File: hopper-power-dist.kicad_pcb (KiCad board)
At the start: 2 copper layers, 28 parts, among them J1 XT90PW-M, J2 B2B-XH-A(LF)(SN), J3 XT60PW-F, J4 XT60PW-F, J5 XT60PW-F, J6 XT60PW-F, J7 XT60PW-F, J8 B2B-XH-A(LF)(SN), SW2 FT_Power_Switch

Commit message: Create basic PCB layout
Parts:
- added D5: LED, LED_SMD:LED_0603_1608Metric, F.Cu at (99.5, 116.0)
- added R4: 22kΩ, Resistor_SMD:R_0603_1608Metric_Pad0.98x0.95mm_HandSolder, F.Cu at (95.3, 116.0)
- added REF**: MountingHole_2.2mm_M2, MountingHole:MountingHole_2.2mm_M2, F.Cu at (59.0, 67.0)
- added REF**: MountingHole_2.2mm_M2, MountingHole:MountingHole_2.2mm_M2, F.Cu at (160.0, 138.0)
- added REF**: MountingHole_2.2mm_M2, MountingHole:MountingHole_2.2mm_M2, F.Cu at (160.0, 67.0)
- added REF**: MountingHole_2.2mm_M2, MountingHole:MountingHole_2.2mm_M2, F.Cu at (59.0, 138.0)
- moved J2 99.2 mm to (76.0, 68.0), turned to -90 degrees
- moved R2 83.3 mm to (90.6, 138.0)
- moved C9 80.1 mm to (97.5, 69.5), turned to 90 degrees
- moved D2 76.3 mm to (101.0, 126.8), turned to -90 degrees
- moved J1 76.2 mm to (145.0, 125.0)
- moved J5 72.9 mm to (72.8, 120.2), turned to -90 degrees
- moved R3 71.4 mm to (95.6, 130.4), turned to -90 degrees
- moved R1 68.8 mm to (101.0, 130.8), turned to -90 degrees
- moved J8 64.7 mm to (117.5, 129.0), turned to 180 degrees
- moved SW2 55.0 mm to (128.8, 123.2), turned to -90 degrees
- moved C5 54.9 mm to (97.5, 80.2), turned to 180 degrees
- moved S1 54.3 mm to (110.0, 117.0), turned to -90 degrees
- moved C7 48.7 mm to (115.9, 69.5), turned to 90 degrees
- moved D4 37.3 mm to (95.6, 126.2), turned to -90 degrees
- moved J6 37.0 mm to (147.8, 102.7), turned to 90 degrees
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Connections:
- J3 pad S1: Net-(J3-PadS1) -> GND
- J3 pad S2: Net-(J3-PadS1) -> GND
- J4 pad S1: Net-(J4-PadS1) -> GND
- J4 pad S2: Net-(J4-PadS1) -> GND
- J5 pad S1: Net-(J5-PadS1) -> GND
- J5 pad S2: Net-(J5-PadS1) -> GND
- J6 pad S1: Net-(J6-PadS1) -> GND
- J6 pad S2: Net-(J6-PadS1) -> GND
- J7 pad S1: Net-(J7-PadS1) -> GND
- J7 pad S2: Net-(J7-PadS1) -> GND
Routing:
- net Net-(J1-PadP): track 0.00 -> 12.9 mm
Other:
- board outline added: 109 x 79 mm

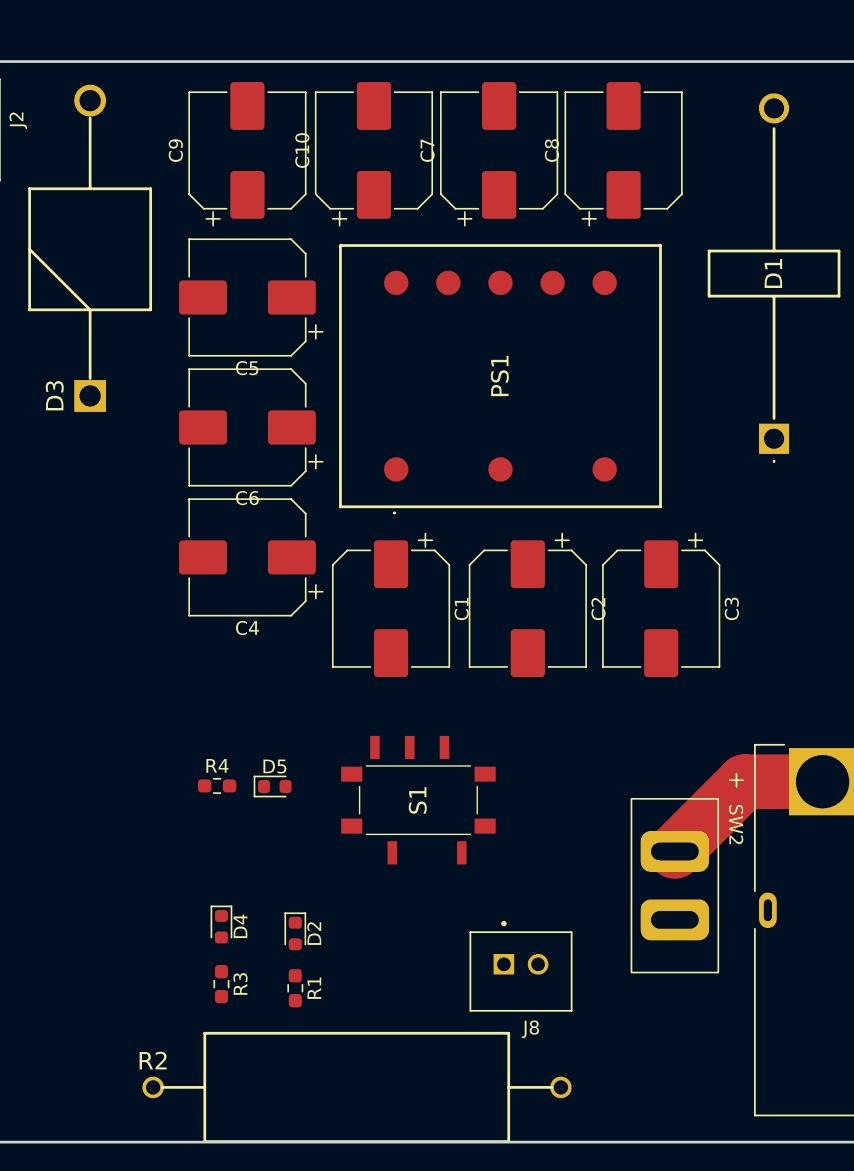
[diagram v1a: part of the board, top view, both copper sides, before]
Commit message: Fix schematic and update 3d models
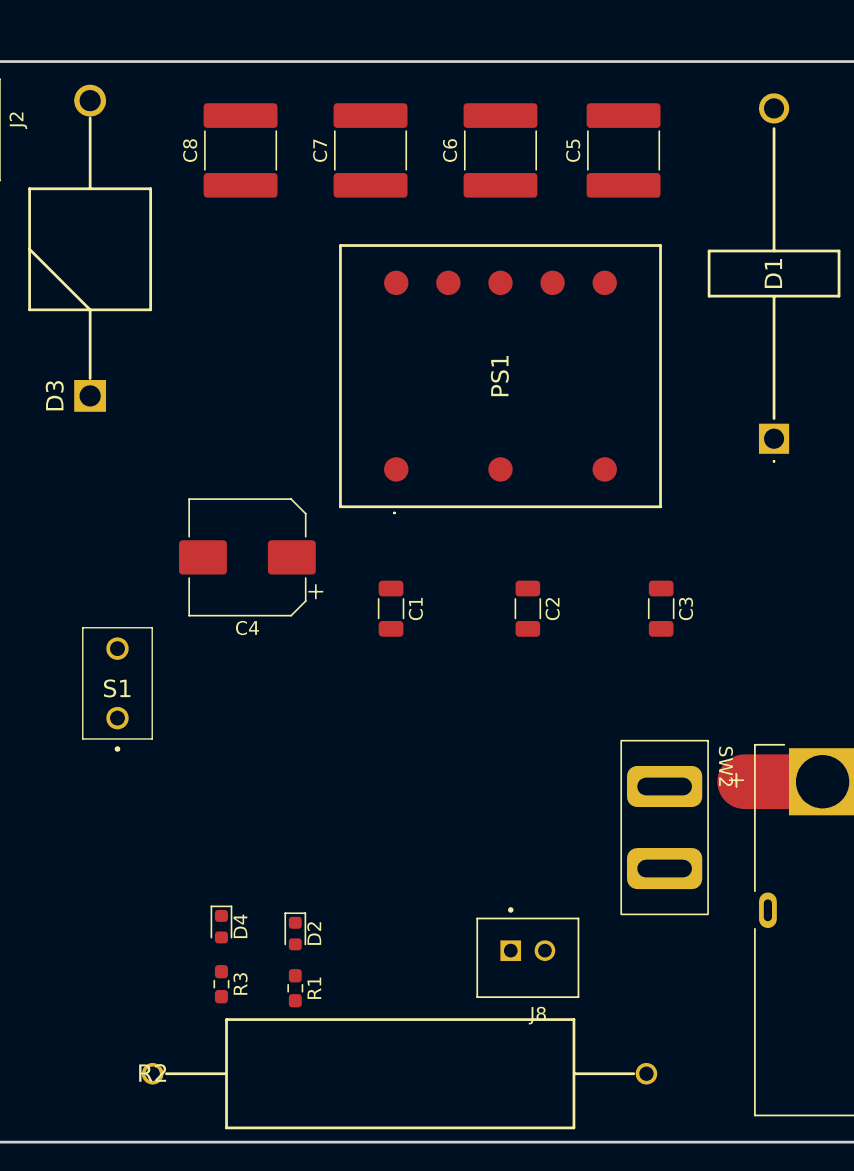
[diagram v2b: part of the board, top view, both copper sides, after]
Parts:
- removed the C5 at (97.5, 80.2)
- removed the C6 at (97.5, 89.8)
- removed D5: LED, LED_SMD:LED_0603_1608Metric
- removed R4: 22kΩ, Resistor_SMD:R_0603_1608Metric_Pad0.98x0.95mm_HandSolder
- C1, C2, C3: footprint Capacitor_SMD:CP_Elec_8x10 -> Capacitor_SMD:C_1206_3216Metric
- C5: renamed from C7; footprint Capacitor_SMD:CP_Elec_8x10 -> Capacitor_SMD:C_2220_5650Metric
- C6: renamed from C8; footprint Capacitor_SMD:CP_Elec_8x10 -> Capacitor_SMD:C_2220_5650Metric
- C7: renamed from C9; footprint Capacitor_SMD:CP_Elec_8x10 -> Capacitor_SMD:C_2220_5650Metric
- C8: renamed from C10; footprint Capacitor_SMD:CP_Elec_8x10 -> Capacitor_SMD:C_2220_5650Metric
- R2: footprint SamacSys_Parts:RESAD5390W86L2222D792 -> benbokser:CW005900R0JB12
- S1: value G3T12AB -> 2MS6T1B3M2QES; footprint SamacSys_Parts:G3T12AB -> SamacSys_Parts:2MS6T1B3M2QES
- moved S1 22.8 mm to (88.0, 111.0), turned to 0 degrees
- moved C8 9.75 mm to (97.0, 69.5)
- moved C5 9.10 mm to (125.0, 69.5)
- moved C6 9.00 mm to (116.0, 69.5)
- moved C7 9.00 mm to (106.5, 69.5)
- moved SW2 4.32 mm to (128.0, 119.0)
- moved J8 1.12 mm to (118.0, 128.0)
- moved R2 1.00 mm to (90.6, 137.0)
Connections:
- S1 pad 1: /HS -> GND
- S1 pad 3: GND -> Net-(PS1-Pad2)
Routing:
- net Net-(J1-PadP): track 12.9 -> 5.70 mm

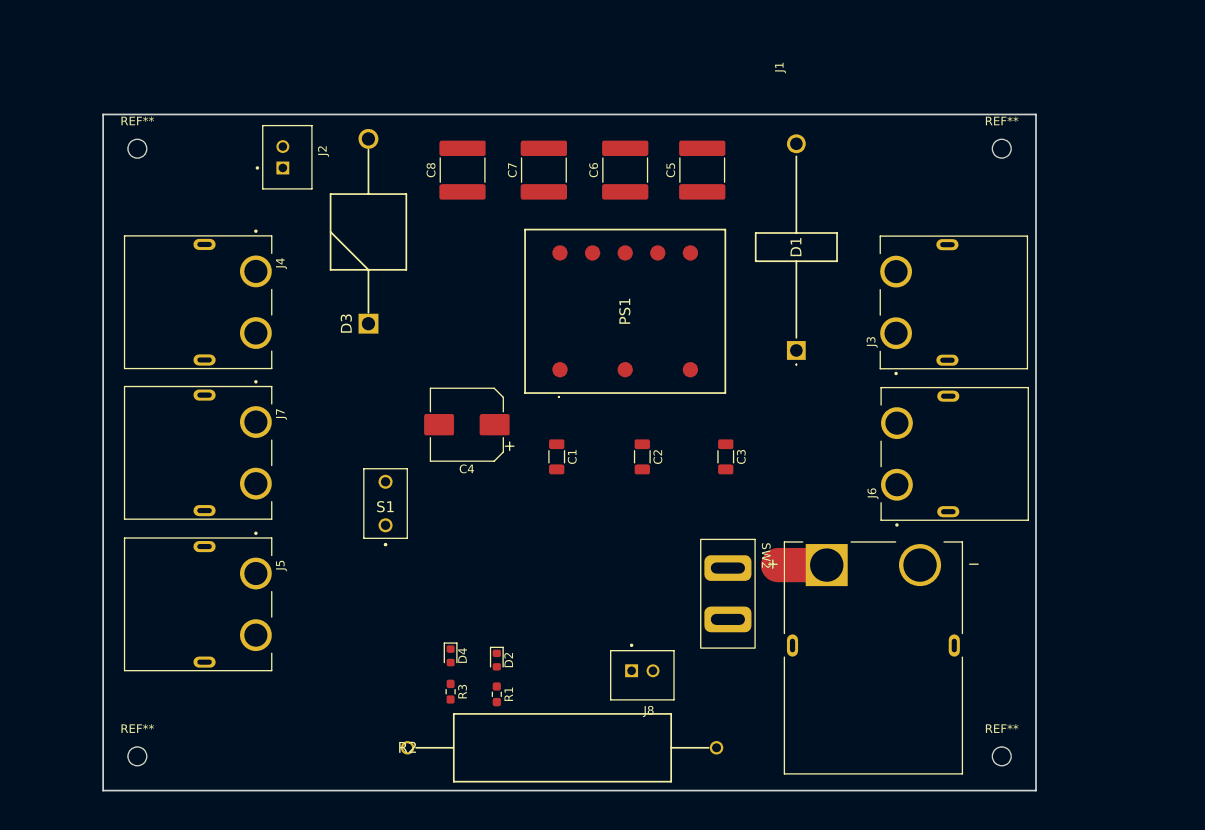
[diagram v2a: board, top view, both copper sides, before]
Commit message: Changed precharge resistor, routed PCB traces and updated 3D models
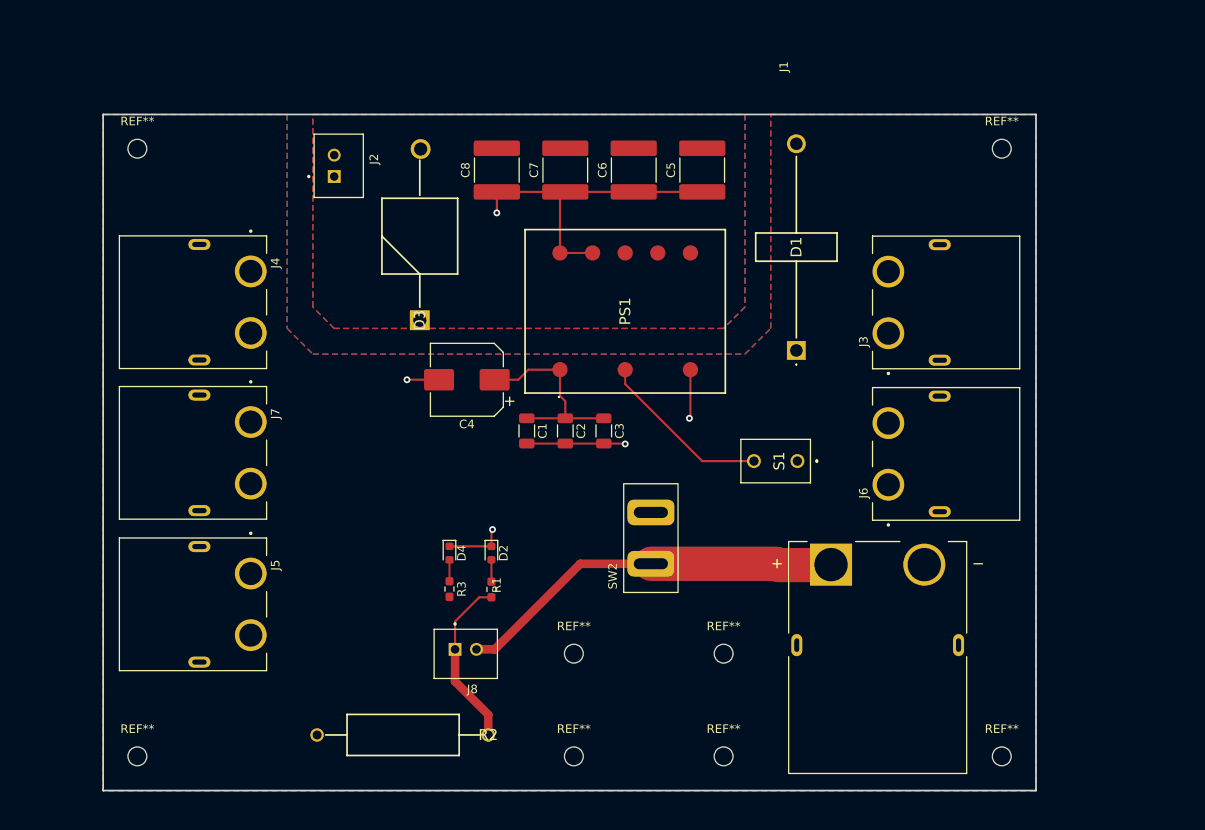
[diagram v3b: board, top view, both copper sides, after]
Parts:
- added REF**: MountingHole_2.2mm_M2, MountingHole:MountingHole_2.2mm_M2, F.Cu at (110.0, 138.0)
- added REF**: MountingHole_2.2mm_M2, MountingHole:MountingHole_2.2mm_M2, F.Cu at (110.0, 126.0)
- added REF**: MountingHole_2.2mm_M2, MountingHole:MountingHole_2.2mm_M2, F.Cu at (127.5, 138.0)
- added REF**: MountingHole_2.2mm_M2, MountingHole:MountingHole_2.2mm_M2, F.Cu at (127.5, 126.0)
- D3: footprint SamacSys_Parts:DIOAD4425W136L885D885 -> benbokser:5KP12A
- R2: value 900Ω -> 365Ω; footprint benbokser:CW005900R0JB12 -> benbokser:AC03000003600JAC00
- moved S1 48.7 mm to (136.1, 103.5), turned to 90 degrees
- moved J8 20.8 mm to (97.4, 125.5)
- moved C3 14.6 mm to (113.5, 100.0)
- moved D2 12.5 mm to (100.4, 114.2)
- moved R1 12.3 mm to (100.4, 118.5)
- moved D4 12.0 mm to (95.5, 114.2)
- moved R3 12.0 mm to (95.5, 118.5)
- moved SW2 11.1 mm to (119.0, 112.5), turned to 90 degrees
- moved R2 9.55 mm to (100.0, 135.5), turned to 180 degrees
- moved C2 9.49 mm to (109.0, 100.0)
- moved J2 6.08 mm to (82.0, 69.0)
- moved D3 6.02 mm to (92.0, 87.0)
- moved C4 5.25 mm to (97.5, 94.0)
- moved C1 4.63 mm to (104.5, 100.0)
- moved C8 4.00 mm to (101.0, 69.5)
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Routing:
- net Net-(J1-PadP): track 5.70 -> 45.1 mm
- net Net-(C5-Pad1): track 0.00 -> 37.7 mm, vias 0 -> 1
- net GND: track 0.00 -> 27.9 mm, vias 0 -> 4
- net /HS: track 0.00 -> 24.1 mm
- net Net-(PS1-Pad2): track 0.00 -> 20.5 mm
- net Net-(J8-Pad1): track 0.00 -> 20.3 mm
- net Net-(D2-Pad2): track 0.00 -> 2.55 mm
- net Net-(D4-Pad2): track 0.00 -> 2.50 mm
- added copper zone on F.Cu, net /-12V
- added copper zone on F.Cu, net /HS
- added copper zone on B.Cu, net GND
- added copper zone on B.Cu, net Net-(C5-Pad1)

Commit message: Improved PCB design and completed DRC
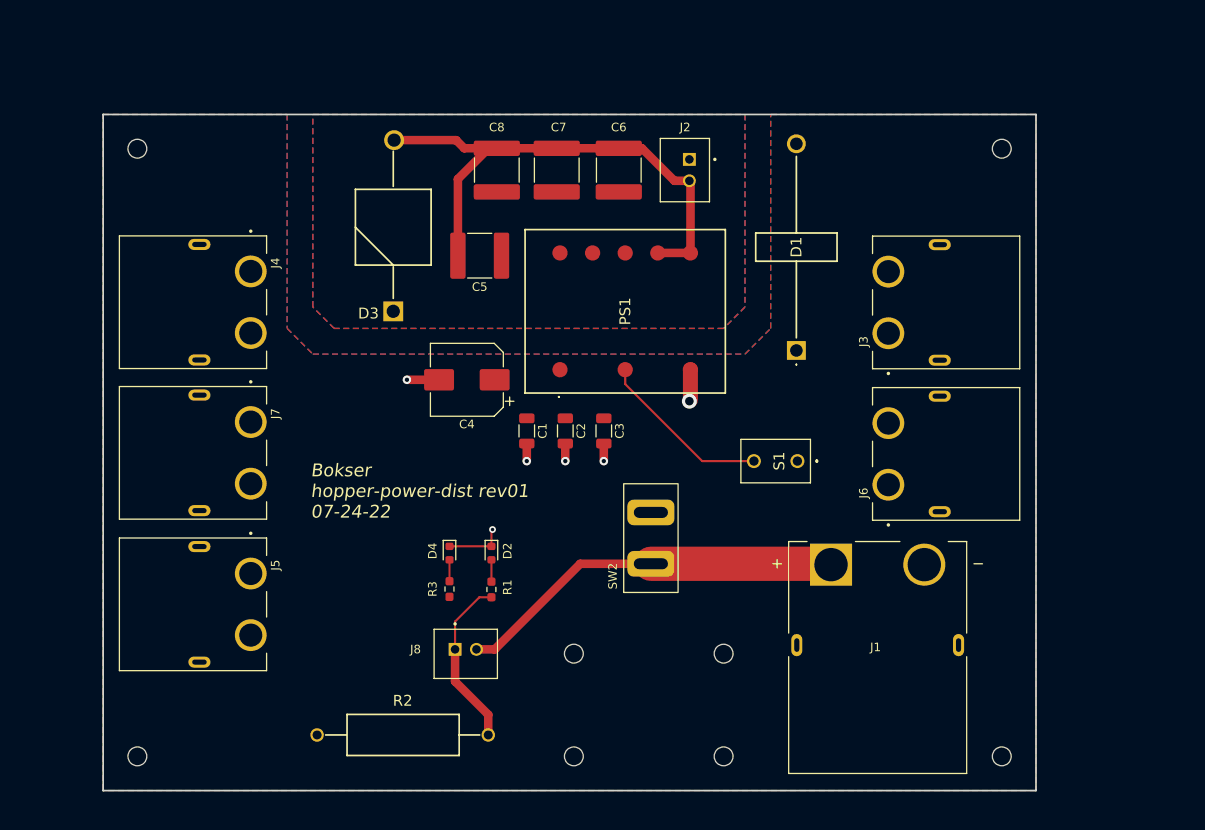
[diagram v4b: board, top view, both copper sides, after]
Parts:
- moved J2 41.5 mm to (123.5, 69.5), turned to 90 degrees
- moved C5 27.9 mm to (99.0, 79.5), turned to 180 degrees
- moved D3 3.27 mm to (88.9, 86.0)
- moved C6 1.75 mm to (115.2, 69.5)
- moved C7 1.00 mm to (108.0, 69.5)
- renumbered REF** to REF
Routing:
- net /-12V: track 0.19 -> 63.7 mm
- net Net-(C5-Pad1): track 37.7 -> 0.45 mm, vias 1 -> 0
- net /HS: track 24.1 -> 0.00 mm
- net GND: track 27.9 -> 20.5 mm, vias 4 -> 6
- added copper zone on B.Cu, net /-12V
- added copper zone on F.Cu, net Net-(C5-Pad1)
- removed copper zone on F.Cu, net /-12V
- removed copper zone on B.Cu, net Net-(C5-Pad1)
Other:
- rule pad_to_mask_clearance: 0 -> 0.0508
- board text added: "Bokser hopper-power-dist rev01 07-24-22"
